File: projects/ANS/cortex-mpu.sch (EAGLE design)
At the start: 4 parts, among them U2 ATSAM3S4AA-AU

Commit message: C
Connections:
- removed net N$1: R1.1, U2.DDM/PB10
- removed net N$3: R2.1, U2.DDP/PB11
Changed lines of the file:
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@@
 </busses>
 <nets>
-<net name="N$1" class="0">
-<segment>
-<pinref part="U2" gate="A" pin="DDM/PB10"/>
-<wire x1="40.64" y1="83.82" x2="33.02" y2="83.82" width="0.1524" layer="91"/>
-<wire x1="33.02" y1="83.82" x2="33.02" y2="55.88" width="0.1524" layer="91"/>
-<wire x1="33.02" y1="55.88" x2="124.46" y2="55.88" width="0.1524" layer="91"/>
-<wire x1="124.46" y1="55.88" x2="149.86" y2="81.28" width="0.1524" layer="91"/>
-<wire x1="149.86" y1="81.28" x2="149.86" y2="119.38" width="0.1524" layer="91"/>
-<wire x1="149.86" y1="119.38" x2="157.48" y2="127" width="0.1524" layer="91"/>
-<pinref part="R1" gate="G$1" pin="1"/>
-<wire x1="157.48" y1="127" x2="167.64" y2="127" width="0.1524" layer="91"/>
-</segment>
-</net>
 <net name="N$2" class="0">
 <segment>
@@
 </segment>
 </net>
-<net name="N$3" class="0">
-<segment>
-<pinref part="U2" gate="A" pin="DDP/PB11"/>
-<wire x1="127" y1="81.28" x2="147.32" y2="101.6" width="0.1524" layer="91"/>
-<wire x1="147.32" y1="101.6" x2="147.32" y2="114.3" width="0.1524" layer="91"/>
-<wire x1="147.32" y1="114.3" x2="154.94" y2="121.92" width="0.1524" layer="91"/>
-<pinref part="R2" gate="G$1" pin="1"/>
-<wire x1="154.94" y1="121.92" x2="167.64" y2="121.92" width="0.1524" layer="91"/>
-</segment>
-</net>

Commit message: Doc
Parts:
- removed U2: ATSAM3S4AA-AU, Atmel_By_element14_Batch_1-00:ATSAM3S4AA-AU
- added U1: AT32UC3B164-AUT, Atmel_By_element14_Batch_1-00:AT32UC3B164-AUT
- R1, R2: value (none) -> 39R
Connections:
- removed net N$4: JP1.D+, R2.2
- new net DM: R1.2
- new net DP: R2.2
- new net GND: JP1.GND, JP1.SHIELD
- new net N$1: JP1.D-, R1.1
- new net PA0: U1.PA00
- new net PA1: U1.PA01
- new net PA10: U1.PA10
- new net PA11: U1.PA11
- new net PA12: U1.PA12
- new net PA13: U1.PA13
- new net PA14: U1.PA14
- new net PA15: U1.PA15
- new net PA16: U1.PA16
- new net PA17: U1.PA17
- new net PA18: U1.PA18
- new net PA19: U1.PA19
- new net PA2: U1.PA02
- new net PA20: U1.PA20
- new net PA21: U1.PA21
- new net PA22: U1.PA22
- new net PA23: U1.PA23
- new net PA24: U1.PA24
- new net PA25: U1.PA25
- new net PA26: JP1.ID, U1.PA26
- new net PA27: U1.PA27
- new net PA3: U1.PA03
- new net PA4: U1.PA04
- new net PA5: U1.PA05
- new net PA6: U1.PA06
- new net PA7: U1.PA07
- new net PA8: U1.PA08
- new net PA9: U1.PA09
- new net VBUS: JP1.VCC
- net N$2: now also JP1.D+, R2.1; no longer JP1.D-, R1.2
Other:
- moved on the sheet: R1, R2

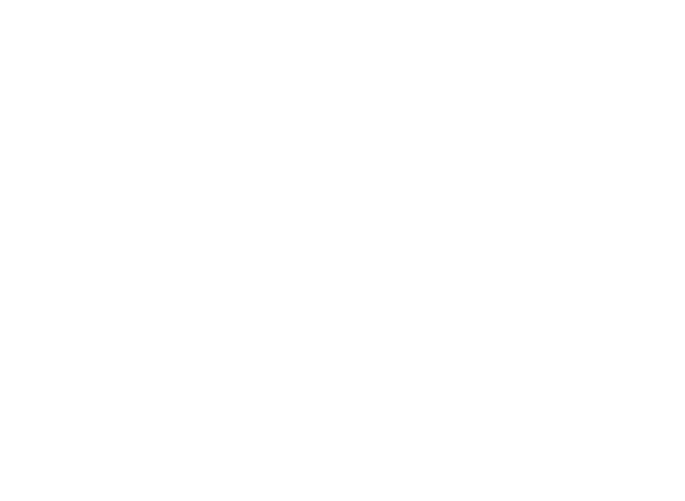
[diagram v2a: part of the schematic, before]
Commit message: Added Power Regulator IC
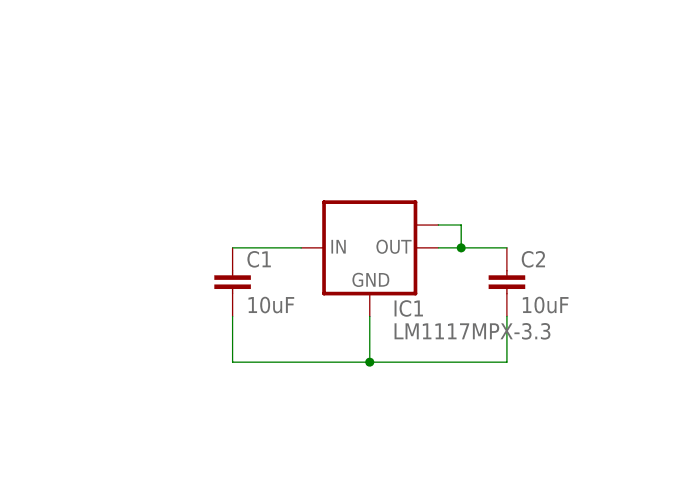
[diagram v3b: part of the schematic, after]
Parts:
- added C1, C2: 10uF, SparkFun-Passives:CAP0603-CAP
- added IC1: LM1117MPX-3.3, lm1117:LM1117MPX-3.3
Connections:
- net VBUS renamed N$3
- new net N$4: C1.2, C2.2, IC1.GND
- new net N$5: C1.1, IC1.IN
- new net N$6: C2.1, IC1.OUT, IC1.OUT1
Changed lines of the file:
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@@
 <setting verticaltext="up"/>
 </settings>
-<grid distance="0.1" unitdist="inch" unit="inch" style="lines" multiple="1" display="no" altdistance="0.01" altunitdist="inch" altunit="inch"/>
+<grid distance="0.1" unitdist="inch" unit="inch" style="dots" multiple="1" display="yes" altdistance="0.01" altunitdist="inch" altunit="inch"/>
 <layers>
 <layer number="1" name="Top" color="4" fill="1" visible="no" active="no"/>
@@
 <part name="U$1" library="SparkFun-Aesthetics" deviceset="AGND" device=""/>
 <part name="SUPPLY2" library="SparkFun-Aesthetics" deviceset="3.3V" device=""/>
+<part name="IC1" library="lm1117" deviceset="LM1117MPX-*" device="" technology="3.3"/>
+<part name="C1" library="SparkFun-Passives" deviceset="CAP" device="0603-CAP" value="10uF"/>
+<part name="C2" library="SparkFun-Passives" deviceset="CAP" device="0603-CAP" value="10uF"/>
 </parts>
 <sheets>
@@
 <instance part="U$1" gate="G$1" x="20.32" y="165.1"/>
 <instance part="SUPPLY2" gate="G$1" x="27.94" y="165.1"/>
+<instance part="IC1" gate="G$1" x="198.12" y="71.12"/>
+<instance part="C1" gate="G$1" x="182.88" y="66.04"/>
+<instance part="C2" gate="G$1" x="213.36" y="66.04"/>
 </instances>
 <busses>
@@
 </segment>
 </net>
-<net name="VBUS" class="0">
+<net name="N$3" class="0">
 <segment>
 <pinref part="JP1" gate="G$1" pin="VCC"/>
@@
 </segment>
 </net>
+<net name="N$4" class="0">
+<segment>
+<pinref part="C1" gate="G$1" pin="2"/>
+<wire x1="182.88" y1="63.5" x2="182.88" y2="58.42" width="0.1524" layer="91"/>
+<wire x1="182.88" y1="58.42" x2="198.12" y2="58.42" width="0.1524" layer="91"/>
+<pinref part="C2" gate="G$1" pin="2"/>
+<wire x1="198.12" y1="58.42" x2="213.36" y2="58.42" width="0.1524" layer="91"/>
+<wire x1="213.36" y1="58.42" x2="213.36" y2="63.5" width="0.1524" layer="91"/>
+<pinref part="IC1" gate="G$1" pin="GND"/>
+<wire x1="198.12" y1="63.5" x2="198.12" y2="58.42" width="0.1524" layer="91"/>
+<junction x="198.12" y="58.42"/>
+</segment>
+</net>
+<net name="N$5" class="0">
+<segment>
+<pinref part="C1" gate="G$1" pin="1"/>
+<pinref part="IC1" gate="G$1" pin="IN"/>
+<wire x1="182.88" y1="71.12" x2="190.5" y2="71.12" width="0.1524" layer="91"/>
+</segment>
+</net>
+<net name="N$6" class="0">
+<segment>
+<pinref part="IC1" gate="G$1" pin="OUT"/>
+<pinref part="C2" gate="G$1" pin="1"/>
+<wire x1="205.74" y1="71.12" x2="208.28" y2="71.12" width="0.1524" layer="91"/>
+<pinref part="IC1" gate="G$1" pin="OUT1"/>
+<wire x1="208.28" y1="71.12" x2="213.36" y2="71.12" width="0.1524" layer="91"/>
+<wire x1="205.74" y1="73.66" x2="208.28" y2="73.66" width="0.1524" layer="91"/>
+<wire x1="208.28" y1="73.66" x2="208.28" y2="71.12" width="0.1524" layer="91"/>
+<junction x="208.28" y="71.12"/>
+</segment>
+</net>

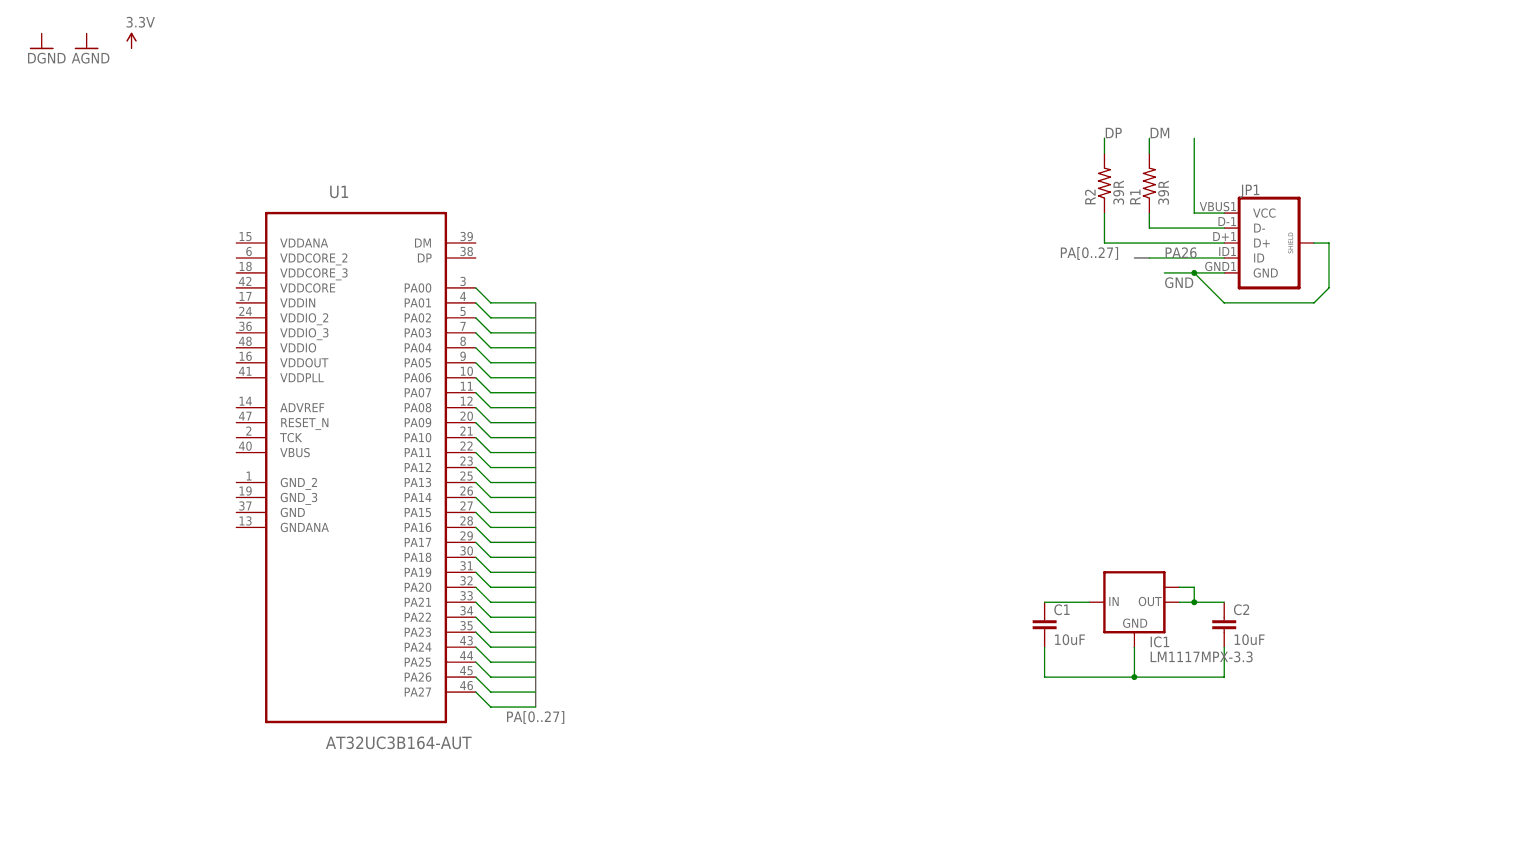
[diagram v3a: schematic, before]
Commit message: Various Net Connections
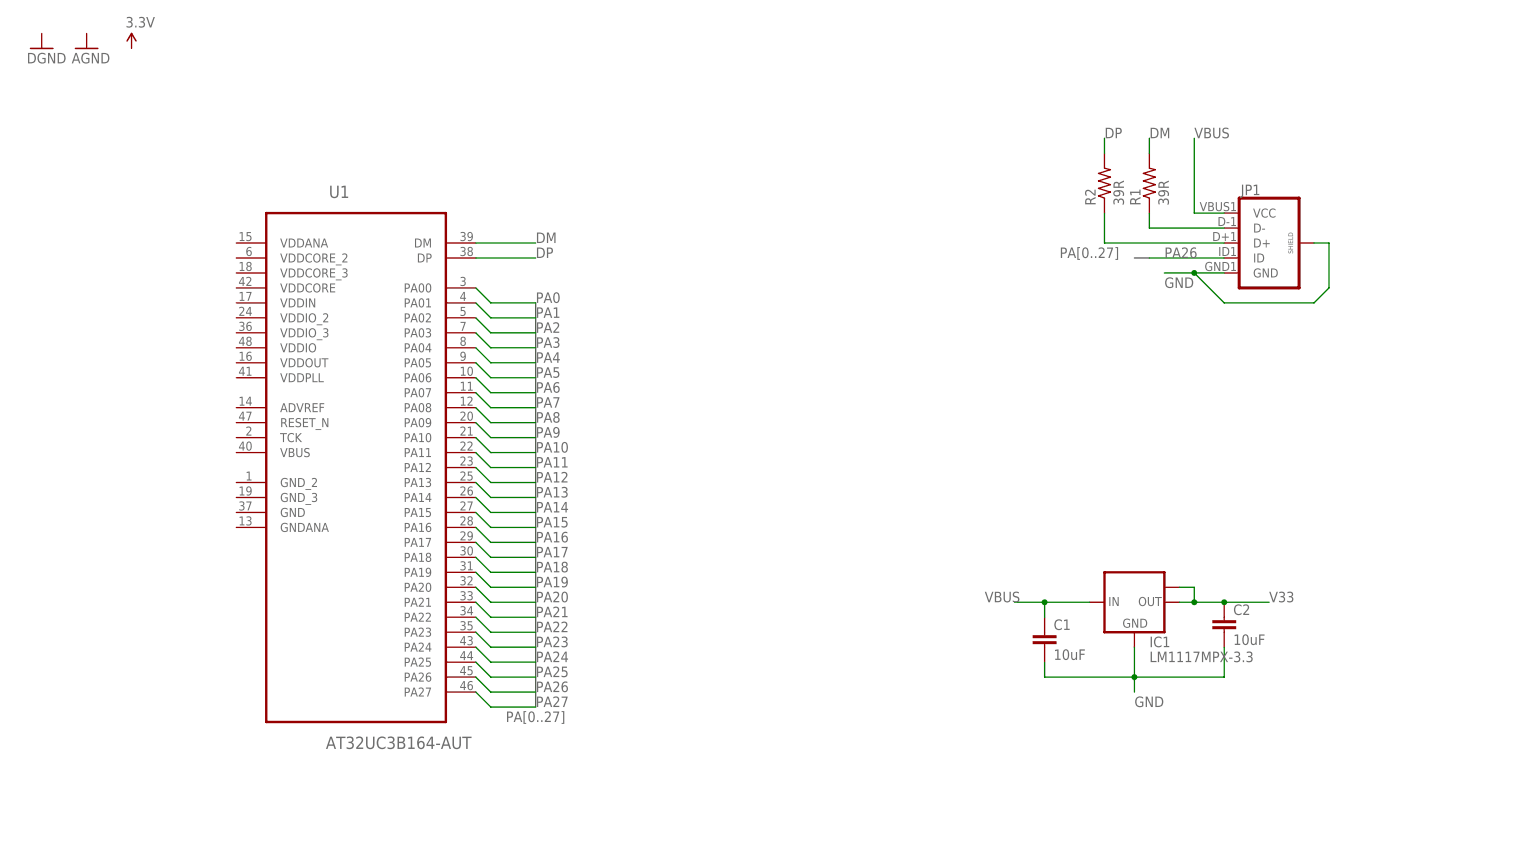
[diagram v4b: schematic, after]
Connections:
- net N$6 renamed V33
- removed net N$3: JP1.VCC
- removed net N$4: C1.2, C2.2, IC1.GND
- removed net N$5: C1.1, IC1.IN
- new net VBUS: C1.1, IC1.IN, JP1.VCC
- net DM: now also U1.DM
- net DP: now also U1.DP
- net GND: now also C1.2, C2.2, IC1.GND
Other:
- moved on the sheet: C1
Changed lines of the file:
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@@
 <instance part="SUPPLY2" gate="G$1" x="27.94" y="165.1"/>
 <instance part="IC1" gate="G$1" x="198.12" y="71.12"/>
-<instance part="C1" gate="G$1" x="182.88" y="66.04"/>
+<instance part="C1" gate="G$1" x="182.88" y="63.5"/>
 <instance part="C2" gate="G$1" x="213.36" y="66.04"/>
 </instances>
@@
 <label x="200.66" y="149.86" size="1.778" layer="95"/>
 </segment>
+<segment>
+<pinref part="U1" gate="A" pin="DM"/>
+<wire x1="86.36" y1="132.08" x2="96.52" y2="132.08" width="0.1524" layer="91"/>
+<label x="96.52" y="132.08" size="1.778" layer="95"/>
+</segment>
 </net>
 <net name="DP" class="0">
@@
 <label x="193.04" y="149.86" size="1.778" layer="95"/>
 </segment>
+<segment>
+<pinref part="U1" gate="A" pin="DP"/>
+<wire x1="86.36" y1="129.54" x2="96.52" y2="129.54" width="0.1524" layer="91"/>
+<label x="96.52" y="129.54" size="1.778" layer="95"/>
+</segment>
 </net>
 <net name="PA0" class="0">
@@
 <wire x1="96.52" y1="121.92" x2="88.9" y2="121.92" width="0.1524" layer="91"/>
 <wire x1="88.9" y1="121.92" x2="86.36" y2="124.46" width="0.1524" layer="91"/>
+<label x="96.52" y="121.92" size="1.778" layer="95"/>
 </segment>
 </net>
@@
 <wire x1="96.52" y1="119.38" x2="88.9" y2="119.38" width="0.1524" layer="91"/>
 <wire x1="88.9" y1="119.38" x2="86.36" y2="121.92" width="0.1524" layer="91"/>
+<label x="96.52" y="119.38" size="1.778" layer="95"/>
 </segment>
 </net>
@@
 <wire x1="96.52" y1="116.84" x2="88.9" y2="116.84" width="0.1524" layer="91"/>
 <wire x1="88.9" y1="116.84" x2="86.36" y2="119.38" width="0.1524" layer="91"/>
+<label x="96.52" y="116.84" size="1.778" layer="95"/>
 </segment>
 </net>
@@
 <wire x1="96.52" y1="114.3" x2="88.9" y2="114.3" width="0.1524" layer="91"/>
 <wire x1="88.9" y1="114.3" x2="86.36" y2="116.84" width="0.1524" layer="91"/>
+<label x="96.52" y="114.3" size="1.778" layer="95"/>
 </segment>
 </net>
@@
 <wire x1="96.52" y1="111.76" x2="88.9" y2="111.76" width="0.1524" layer="91"/>
 <wire x1="88.9" y1="111.76" x2="86.36" y2="114.3" width="0.1524" layer="91"/>
+<label x="96.52" y="111.76" size="1.778" layer="95"/>
 </segment>
 </net>
@@
 <wire x1="96.52" y1="109.22" x2="88.9" y2="109.22" width="0.1524" layer="91"/>
 <wire x1="88.9" y1="109.22" x2="86.36" y2="111.76" width="0.1524" layer="91"/>
+<label x="96.52" y="109.22" size="1.778" layer="95"/>
 </segment>
 </net>
@@
 <wire x1="96.52" y1="106.68" x2="88.9" y2="106.68" width="0.1524" layer="91"/>
 <wire x1="88.9" y1="106.68" x2="86.36" y2="109.22" width="0.1524" layer="91"/>
+<label x="96.52" y="106.68" size="1.778" layer="95"/>
 </segment>
 </net>
@@
 <wire x1="96.52" y1="104.14" x2="88.9" y2="104.14" width="0.1524" layer="91"/>
 <wire x1="88.9" y1="104.14" x2="86.36" y2="106.68" width="0.1524" layer="91"/>
+<label x="96.52" y="104.14" size="1.778" layer="95"/>
 </segment>
 </net>
@@
 <wire x1="96.52" y1="101.6" x2="88.9" y2="101.6" width="0.1524" layer="91"/>
 <wire x1="88.9" y1="101.6" x2="86.36" y2="104.14" width="0.1524" layer="91"/>
+<label x="96.52" y="101.6" size="1.778" layer="95"/>
 </segment>
 </net>
@@
 <wire x1="96.52" y1="99.06" x2="88.9" y2="99.06" width="0.1524" layer="91"/>
 <wire x1="88.9" y1="99.06" x2="86.36" y2="101.6" width="0.1524" layer="91"/>
+<label x="96.52" y="99.06" size="1.778" layer="95"/>
 </segment>
 </net>
@@
 <wire x1="96.52" y1="96.52" x2="88.9" y2="96.52" width="0.1524" layer="91"/>
 <wire x1="88.9" y1="96.52" x2="86.36" y2="99.06" width="0.1524" layer="91"/>
+<label x="96.52" y="96.52" size="1.778" layer="95"/>
 </segment>
 </net>
@@
 <wire x1="96.52" y1="93.98" x2="88.9" y2="93.98" width="0.1524" layer="91"/>
 <wire x1="88.9" y1="93.98" x2="86.36" y2="96.52" width="0.1524" layer="91"/>
+<label x="96.52" y="93.98" size="1.778" layer="95"/>
 </segment>
 </net>
@@
 <wire x1="96.52" y1="91.44" x2="88.9" y2="91.44" width="0.1524" layer="91"/>
 <wire x1="88.9" y1="91.44" x2="86.36" y2="93.98" width="0.1524" layer="91"/>
+<label x="96.52" y="91.44" size="1.778" layer="95"/>
 </segment>
 </net>
@@
 <wire x1="96.52" y1="88.9" x2="88.9" y2="88.9" width="0.1524" layer="91"/>
 <wire x1="88.9" y1="88.9" x2="86.36" y2="91.44" width="0.1524" layer="91"/>
+<label x="96.52" y="88.9" size="1.778" layer="95"/>
 </segment>
 </net>
@@
 <wire x1="96.52" y1="86.36" x2="88.9" y2="86.36" width="0.1524" layer="91"/>
 <wire x1="88.9" y1="86.36" x2="86.36" y2="88.9" width="0.1524" layer="91"/>
+<label x="96.52" y="86.36" size="1.778" layer="95"/>
 </segment>
 </net>
@@
 <wire x1="96.52" y1="83.82" x2="88.9" y2="83.82" width="0.1524" layer="91"/>
 <wire x1="88.9" y1="83.82" x2="86.36" y2="86.36" width="0.1524" layer="91"/>
+<label x="96.52" y="83.82" size="1.778" layer="95"/>
 </segment>
 </net>
@@
 <wire x1="96.52" y1="81.28" x2="88.9" y2="81.28" width="0.1524" layer="91"/>
 <wire x1="88.9" y1="81.28" x2="86.36" y2="83.82" width="0.1524" layer="91"/>
+<label x="96.52" y="81.28" size="1.778" layer="95"/>
 </segment>
 </net>
@@
 <wire x1="96.52" y1="78.74" x2="88.9" y2="78.74" width="0.1524" layer="91"/>
 <wire x1="88.9" y1="78.74" x2="86.36" y2="81.28" width="0.1524" layer="91"/>
+<label x="96.52" y="78.74" size="1.778" layer="95"/>
 </segment>
 </net>
@@
 <wire x1="96.52" y1="76.2" x2="88.9" y2="76.2" width="0.1524" layer="91"/>
 <wire x1="88.9" y1="76.2" x2="86.36" y2="78.74" width="0.1524" layer="91"/>
+<label x="96.52" y="76.2" size="1.778" layer="95"/>
 </segment>
 </net>
@@
 <wire x1="96.52" y1="73.66" x2="88.9" y2="73.66" width="0.1524" layer="91"/>
 <wire x1="88.9" y1="73.66" x2="86.36" y2="76.2" width="0.1524" layer="91"/>
+<label x="96.52" y="73.66" size="1.778" layer="95"/>
 </segment>
 </net>
@@
 <wire x1="96.52" y1="71.12" x2="88.9" y2="71.12" width="0.1524" layer="91"/>
 <wire x1="88.9" y1="71.12" x2="86.36" y2="73.66" width="0.1524" layer="91"/>
+<label x="96.52" y="71.12" size="1.778" layer="95"/>
 </segment>
 </net>
@@
 <wire x1="96.52" y1="68.58" x2="88.9" y2="68.58" width="0.1524" layer="91"/>
 <wire x1="88.9" y1="68.58" x2="86.36" y2="71.12" width="0.1524" layer="91"/>
+<label x="96.52" y="68.58" size="1.778" layer="95"/>
 </segment>
 </net>
@@
 <wire x1="96.52" y1="66.04" x2="88.9" y2="66.04" width="0.1524" layer="91"/>
 <wire x1="88.9" y1="66.04" x2="86.36" y2="68.58" width="0.1524" layer="91"/>
+<label x="96.52" y="66.04" size="1.778" layer="95"/>
 </segment>
 </net>
@@
 <wire x1="96.52" y1="63.5" x2="88.9" y2="63.5" width="0.1524" layer="91"/>
 <wire x1="88.9" y1="63.5" x2="86.36" y2="66.04" width="0.1524" layer="91"/>
+<label x="96.52" y="63.5" size="1.778" layer="95"/>
 </segment>
 </net>
@@
 <wire x1="96.52" y1="60.96" x2="88.9" y2="60.96" width="0.1524" layer="91"/>
 <wire x1="88.9" y1="60.96" x2="86.36" y2="63.5" width="0.1524" layer="91"/>
+<label x="96.52" y="60.96" size="1.778" layer="95"/>
 </segment>
 </net>
@@
 <wire x1="96.52" y1="58.42" x2="88.9" y2="58.42" width="0.1524" layer="91"/>
 <wire x1="88.9" y1="58.42" x2="86.36" y2="60.96" width="0.1524" layer="91"/>
+<label x="96.52" y="58.42" size="1.778" layer="95"/>
 </segment>
 </net>
@@
 <wire x1="96.52" y1="55.88" x2="88.9" y2="55.88" width="0.1524" layer="91"/>
 <wire x1="88.9" y1="55.88" x2="86.36" y2="58.42" width="0.1524" layer="91"/>
+<label x="96.52" y="55.88" size="1.778" layer="95"/>
 </segment>
 <segment>
@@
 <wire x1="96.52" y1="53.34" x2="88.9" y2="53.34" width="0.1524" layer="91"/>
 <wire x1="88.9" y1="53.34" x2="86.36" y2="55.88" width="0.1524" layer="91"/>
+<label x="96.52" y="53.34" size="1.778" layer="95"/>
 </segment>
 </net>
@@
 <label x="203.2" y="124.46" size="1.778" layer="95"/>
 </segment>
-</net>
-<net name="N$3" class="0">
-<segment>
-<pinref part="JP1" gate="G$1" pin="VCC"/>
-<wire x1="213.36" y1="137.16" x2="208.28" y2="137.16" width="0.1524" layer="91"/>
-<wire x1="208.28" y1="137.16" x2="208.28" y2="149.86" width="0.1524" layer="91"/>
-</segment>
-</net>
-<net name="N$4" class="0">
 <segment>
 <pinref part="C1" gate="G$1" pin="2"/>
-<wire x1="182.88" y1="63.5" x2="182.88" y2="58.42" width="0.1524" layer="91"/>
+<wire x1="182.88" y1="60.96" x2="182.88" y2="58.42" width="0.1524" layer="91"/>
 <wire x1="182.88" y1="58.42" x2="198.12" y2="58.42" width="0.1524" layer="91"/>
 <pinref part="C2" gate="G$1" pin="2"/>
@@
 <wire x1="198.12" y1="63.5" x2="198.12" y2="58.42" width="0.1524" layer="91"/>
 <junction x="198.12" y="58.42"/>
-</segment>
-</net>
-<net name="N$5" class="0">
-<segment>
+<wire x1="198.12" y1="58.42" x2="198.12" y2="55.88" width="0.1524" layer="91"/>
+<label x="198.12" y="53.34" size="1.778" layer="95"/>
+</segment>
+</net>
+<net name="VBUS" class="0">
+<segment>
+<pinref part="JP1" gate="G$1" pin="VCC"/>
+<wire x1="213.36" y1="137.16" x2="208.28" y2="137.16" width="0.1524" layer="91"/>
+<wire x1="208.28" y1="137.16" x2="208.28" y2="149.86" width="0.1524" layer="91"/>
+<label x="208.28" y="149.86" size="1.778" layer="95"/>
+</segment>
+<segment>
+<pinref part="IC1" gate="G$1" pin="IN"/>
+<wire x1="190.5" y1="71.12" x2="182.88" y2="71.12" width="0.1524" layer="91"/>
 <pinref part="C1" gate="G$1" pin="1"/>
-<pinref part="IC1" gate="G$1" pin="IN"/>
-<wire x1="182.88" y1="71.12" x2="190.5" y2="71.12" width="0.1524" layer="91"/>
-</segment>
-</net>
-<net name="N$6" class="0">
+<wire x1="182.88" y1="71.12" x2="182.88" y2="68.58" width="0.1524" layer="91"/>
+<wire x1="182.88" y1="71.12" x2="177.8" y2="71.12" width="0.1524" layer="91"/>
+<junction x="182.88" y="71.12"/>
+<label x="172.72" y="71.12" size="1.778" layer="95"/>
+</segment>
+</net>
+<net name="V33" class="0">
 <segment>
 <pinref part="IC1" gate="G$1" pin="OUT"/>
@@
 <wire x1="208.28" y1="73.66" x2="208.28" y2="71.12" width="0.1524" layer="91"/>
 <junction x="208.28" y="71.12"/>
-</segment>
-</net>
+<wire x1="213.36" y1="71.12" x2="220.98" y2="71.12" width="0.1524" layer="91"/>
+<junction x="213.36" y="71.12"/>
+<label x="220.98" y="71.12" size="1.778" layer="95"/>
+</segment>
+</net>
